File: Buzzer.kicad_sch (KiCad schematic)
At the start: 0 parts

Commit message: Pin out completion
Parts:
- added LS1: Speaker, symbol Device:Speaker
- added Q1: MMBT5551L, Package_TO_SOT_SMD:SOT-23, symbol Transistor_BJT:MMBT5551L
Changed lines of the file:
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@@
 		(comment 1 "天計")
 	)
+	(symbol
+		(lib_id "Transistor_BJT:MMBT5551L")
+		(at 119.38 101.6 0)
+		(unit 1)
+		(exclude_from_sim no)
+		(in_bom yes)
+		(on_board yes)
+		(dnp no)
+		(fields_autoplaced yes)
+		(property "Reference" "Q1"
+			(at 124.46 100.3299 0)
+			(effects
+				(font
+					(size 1.27 1.27)
+				)
+				(justify left)
+			)
+		)
+		(property "Value" "MMBT5551L"
+			(at 124.46 102.8699 0)
+			(effects
+				(font
+					(size 1.27 1.27)
+				)
+				(justify left)
+			)
+		)
+		(property "Footprint" "Package_TO_SOT_SMD:SOT-23"
+			(at 124.46 103.505 0)
+			(effects
+				(font
+					(size 1.27 1.27)
+					(italic yes)
+				)
+				(justify left)
+				(hide yes)
+			)
+		)
+		(property "Datasheet" "www.onsemi.com/pub/Collateral/MMBT5550LT1-D.PDF"
+			(at 119.38 101.6 0)
+			(effects
+				(font
+					(size 1.27 1.27)
+				)
+				(justify left)
+				(hide yes)
+			)
+		)
+		(property "Description" "0.6A Ic, 160V Vce, NPN Transistor, SOT-23"
+			(at 119.38 101.6 0)
+			(effects
+				(font
+					(size 1.27 1.27)
+				)
+				(hide yes)
+			)
+		)
+		(property "Sim.Device" "NPN"
+			(at 119.38 101.6 0)
+			(effects
+				(font
+					(size 1.27 1.27)
+				)
+				(hide yes)
+			)
+		)
+		(property "Sim.Pins" "1=B 2=E 3=C"
+			(at 119.38 101.6 0)
+			(effects
+				(font
+					(size 1.27 1.27)
+				)
+				(hide yes)
+			)
+		)
+		(pin "1"
+		)
+		(pin "3"
+		)
+		(pin "2"
+		)
+		(instances
+			(project ""
+				(path "/c9a8ff63-a0d1-4125-9dd1-40fb53daf536/fa1772ae-d612-479d-9fc0-6f13b32ea30c"
+					(reference "Q1")
+					(unit 1)
+				)
+			)
+		)
+	)
+	(symbol
+		(lib_id "Device:Speaker")
+		(at 129.54 74.93 0)
+		(unit 1)
+		(exclude_from_sim no)
+		(in_bom yes)
+		(on_board yes)
+		(dnp no)
+		(fields_autoplaced yes)
+		(property "Reference" "LS1"
+			(at 134.62 74.9299 0)
+			(effects
+				(font
+					(size 1.27 1.27)
+				)
+				(justify left)
+			)
+		)
+		(property "Value" "Speaker"
+			(at 134.62 77.4699 0)
+			(effects
+				(font
+					(size 1.27 1.27)
+				)
+				(justify left)
+			)
+		)
+		(property "Footprint" ""
+			(at 129.54 80.01 0)
+			(effects
+				(font
+					(size 1.27 1.27)
+				)
+				(hide yes)
+			)
+		)
+		(property "Datasheet" "~"
+			(at 129.286 76.2 0)
+			(effects
+				(font
+					(size 1.27 1.27)
+				)
+				(hide yes)
+			)
+		)
+		(property "Description" "Speaker"
+			(at 129.54 74.93 0)
+			(effects
+				(font
+					(size 1.27 1.27)
+				)
+				(hide yes)
+			)
+		)
+		(pin "1"
+		)
+		(pin "2"
+		)
+		(instances
+			(project ""
+				(path "/c9a8ff63-a0d1-4125-9dd1-40fb53daf536/fa1772ae-d612-479d-9fc0-6f13b32ea30c"
+					(reference "LS1")
+					(unit 1)
+				)
+			)
+		)
+	)
 )

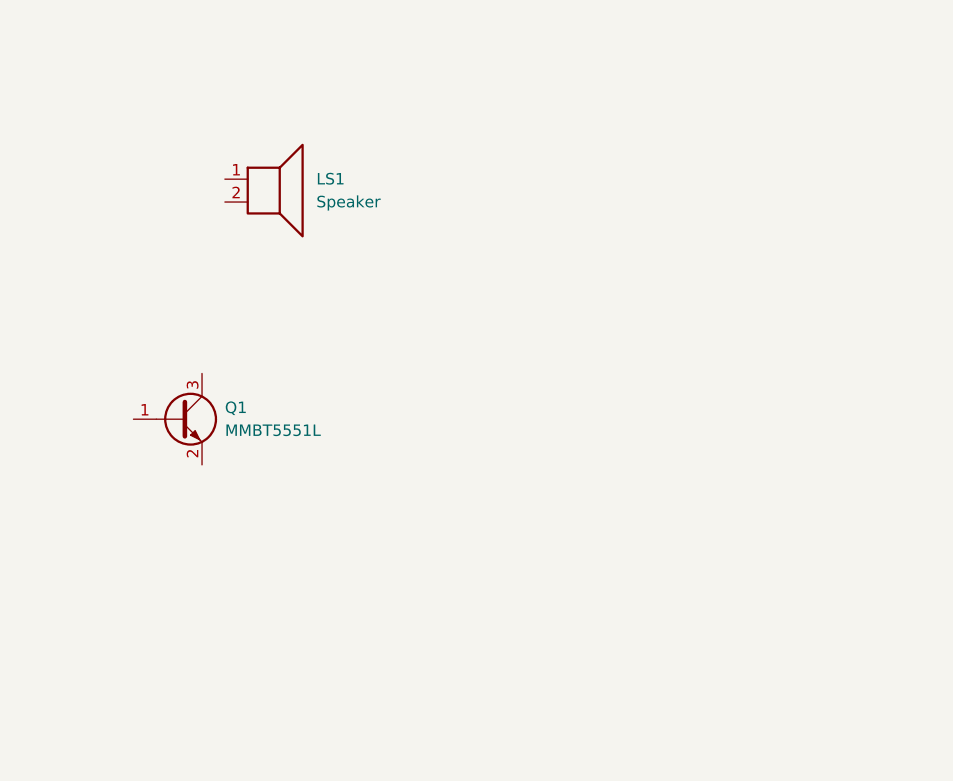
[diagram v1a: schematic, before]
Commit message: buzzer and ambient light sensor added
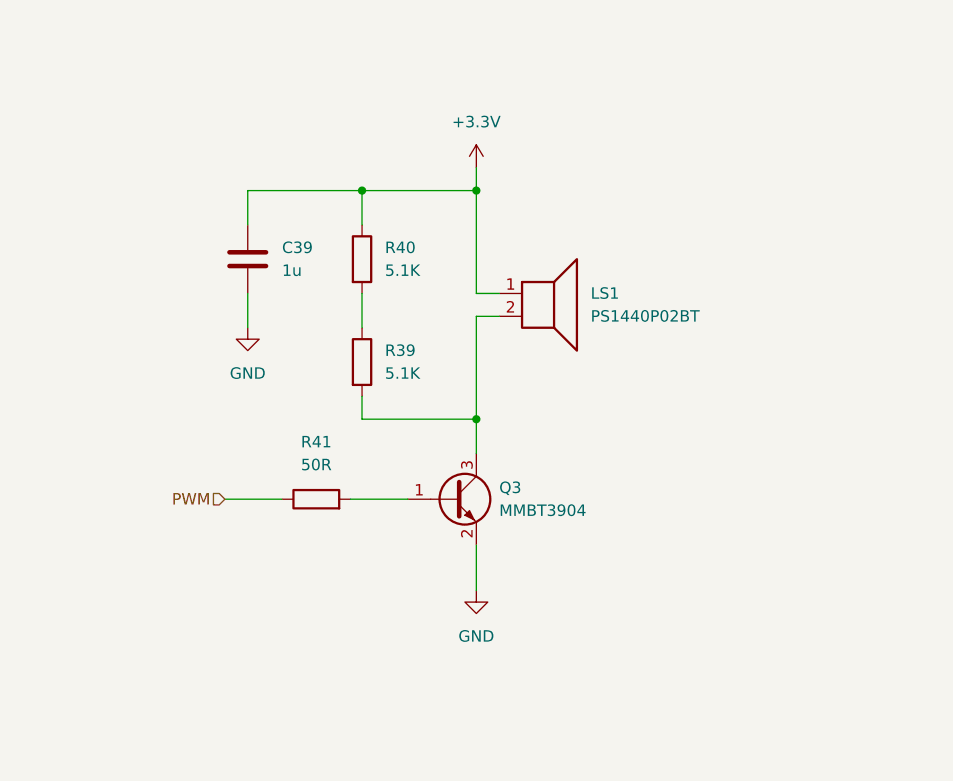
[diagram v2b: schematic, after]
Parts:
- removed Q1: MMBT5551L, Package_TO_SOT_SMD:SOT-23, symbol Transistor_BJT:MMBT5551L
- added C39: 1u, Capacitor_SMD:C_0603_1608Metric, symbol Device:C
- added Q3: MMBT3904, Package_TO_SOT_SMD:SOT-23, symbol Transistor_BJT:MMBT3904
- added R39, R40: 5.1K, Resistor_SMD:R_0402_1005Metric, symbol Device:R
- added R41: 50R, symbol Device:R
- LS1: value Speaker -> PS1440P02BT; footprint (none) -> precision_clock:TDK PS1440P02BT
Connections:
- net +3.3V: now reaches LS1.1
- net +3.3V: now also C39.1, R40.1
- net at LS1.2: now also Q3.3 (C), R39.2
- new net: Q3.1 (B), R41.2
- new net: R39.1, R40.2
- new net GND: C39.2, Q3.2 (E)
- new net PWM: R41.1
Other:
- moved on the sheet: LS1

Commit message: addition of BME690
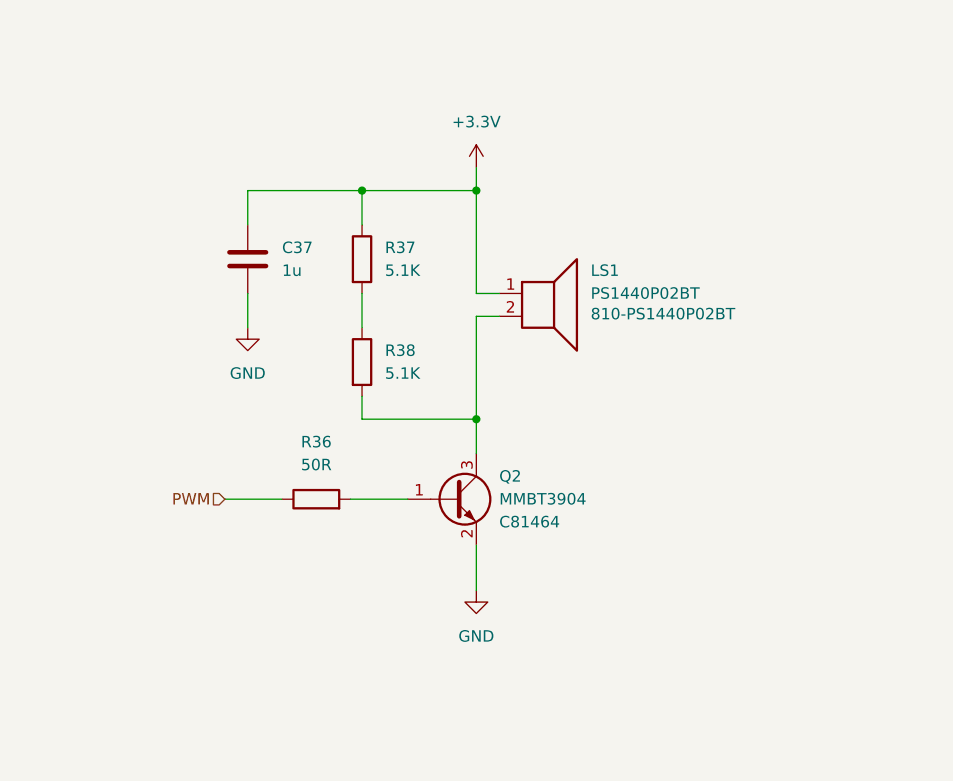
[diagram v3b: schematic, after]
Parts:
- LS1: Mouser (none) -> 810-PS1440P02BT
- Q2: renamed from Q3; LCSC (none) -> C81464
- R36: renamed from R41; footprint (none) -> Resistor_SMD:R_0402_1005Metric
- renumbered C39 to C37, R40 to R37, R39 to R38
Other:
- title: (none) -> Buzzer
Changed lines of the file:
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@@
 	(paper "A4")
 	(title_block
-		(date "2026-01-25")
+		(title "Buzzer")
+		(date "2026-01-27")
 		(rev "v0.0")
 		(company "TJ71PL")
 		(comment 1 "天計")
+		(comment 4 "Final verification incomplete")
 	)
 	(junction
@@
 		(on_board yes)
 		(dnp no)
-		(fields_autoplaced yes)
-		(property "Reference" "Q3"
-			(at 154.94 109.2199 0)
+		(property "Reference" "Q2"
+			(at 154.94 107.9501 0)
 			(effects
 				(font
@@
 		)
 		(property "Value" "MMBT3904"
-			(at 154.94 111.7599 0)
+			(at 154.94 110.49 0)
 			(effects
 				(font
@@
 			)
 		)
+		(property "LCSC" "C81464"
+			(at 154.94 113.0301 0)
+			(effects
+				(font
+					(size 1.27 1.27)
+				)
+				(justify left)
+			)
+		)
 		(pin "2"
 		)
@@
 			(project ""
 				(path "/c9a8ff63-a0d1-4125-9dd1-40fb53daf536/fa1772ae-d612-479d-9fc0-6f13b32ea30c"
-					(reference "Q3")
+					(reference "Q2")
 					(unit 1)
 				)
@@
 		(dnp no)
 		(fields_autoplaced yes)
-		(property "Reference" "R41"
+		(property "Reference" "R36"
 			(at 134.62 104.14 90)
 			(effects
@@
 			)
 		)
-		(property "Footprint" ""
+		(property "Footprint" "Resistor_SMD:R_0402_1005Metric"
 			(at 134.62 112.268 90)
 			(effects
@@
 			(project ""
 				(path "/c9a8ff63-a0d1-4125-9dd1-40fb53daf536/fa1772ae-d612-479d-9fc0-6f13b32ea30c"
-					(reference "R41")
+					(reference "R36")
 					(unit 1)
 				)
@@
 		(dnp no)
 		(fields_autoplaced yes)
-		(property "Reference" "C39"
+		(property "Reference" "C37"
 			(at 130.81 82.5499 0)
 			(effects
@@
 			(project "Precision Clock"
 				(path "/c9a8ff63-a0d1-4125-9dd1-40fb53daf536/fa1772ae-d612-479d-9fc0-6f13b32ea30c"
-					(reference "C39")
+					(reference "C37")
 					(unit 1)
 				)
@@
 		(dnp no)
 		(fields_autoplaced yes)
-		(property "Reference" "#PWR098"
+		(property "Reference" "#PWR097"
 			(at 127 97.79 0)
 			(effects
@@
 			(project "Precision Clock"
 				(path "/c9a8ff63-a0d1-4125-9dd1-40fb53daf536/fa1772ae-d612-479d-9fc0-6f13b32ea30c"
-					(reference "#PWR098")
+					(reference "#PWR097")
 					(unit 1)
 				)
@@
 		(on_board yes)
 		(dnp no)
-		(fields_autoplaced yes)
 		(property "Reference" "LS1"
-			(at 165.1 87.6299 0)
+			(at 165.1 85.09 0)
 			(effects
 				(font
@@
 		)
 		(property "Value" "PS1440P02BT"
-			(at 165.1 90.1699 0)
+			(at 165.1 87.63 0)
 			(effects
 				(font
@@
 			)
 		)
+		(property "Mouser" "810-PS1440P02BT"
+			(at 165.1 89.9161 0)
+			(effects
+				(font
+					(size 1.27 1.27)
+				)
+				(justify left)
+			)
+		)
 		(pin "1"
 		)
@@
 		(dnp no)
 		(fields_autoplaced yes)
-		(property "Reference" "#PWR011"
+		(property "Reference" "#PWR0101"
 			(at 152.4 127 0)
 			(effects
@@
 			(project ""
 				(path "/c9a8ff63-a0d1-4125-9dd1-40fb53daf536/fa1772ae-d612-479d-9fc0-6f13b32ea30c"
-					(reference "#PWR011")
+					(reference "#PWR0101")
 					(unit 1)
 				)
@@
 		(dnp no)
 		(fields_autoplaced yes)
-		(property "Reference" "#PWR020"
+		(property "Reference" "#PWR098"
 			(at 152.4 77.47 0)
 			(effects
@@
 			(project ""
 				(path "/c9a8ff63-a0d1-4125-9dd1-40fb53daf536/fa1772ae-d612-479d-9fc0-6f13b32ea30c"
-					(reference "#PWR020")
+					(reference "#PWR098")
 					(unit 1)
 				)
@@
 		(dnp no)
 		(fields_autoplaced yes)
-		(property "Reference" "R40"
+		(property "Reference" "R37"
 			(at 142.24 82.5499 0)
 			(effects
@@
 			(project "Precision Clock"
 				(path "/c9a8ff63-a0d1-4125-9dd1-40fb53daf536/fa1772ae-d612-479d-9fc0-6f13b32ea30c"
-					(reference "R40")
+					(reference "R37")
 					(unit 1)
 				)
@@
 		(dnp no)
 		(fields_autoplaced yes)
-		(property "Reference" "R39"
+		(property "Reference" "R38"
 			(at 142.24 93.9799 0)
 			(effects
@@
 			(project "Precision Clock"
 				(path "/c9a8ff63-a0d1-4125-9dd1-40fb53daf536/fa1772ae-d612-479d-9fc0-6f13b32ea30c"
-					(reference "R39")
-					(unit 1)
-				)
+					(reference "R38")
+					(unit 1)
+				)

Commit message: Verification
- changed the piezo electric speaker.
- verified some schematics
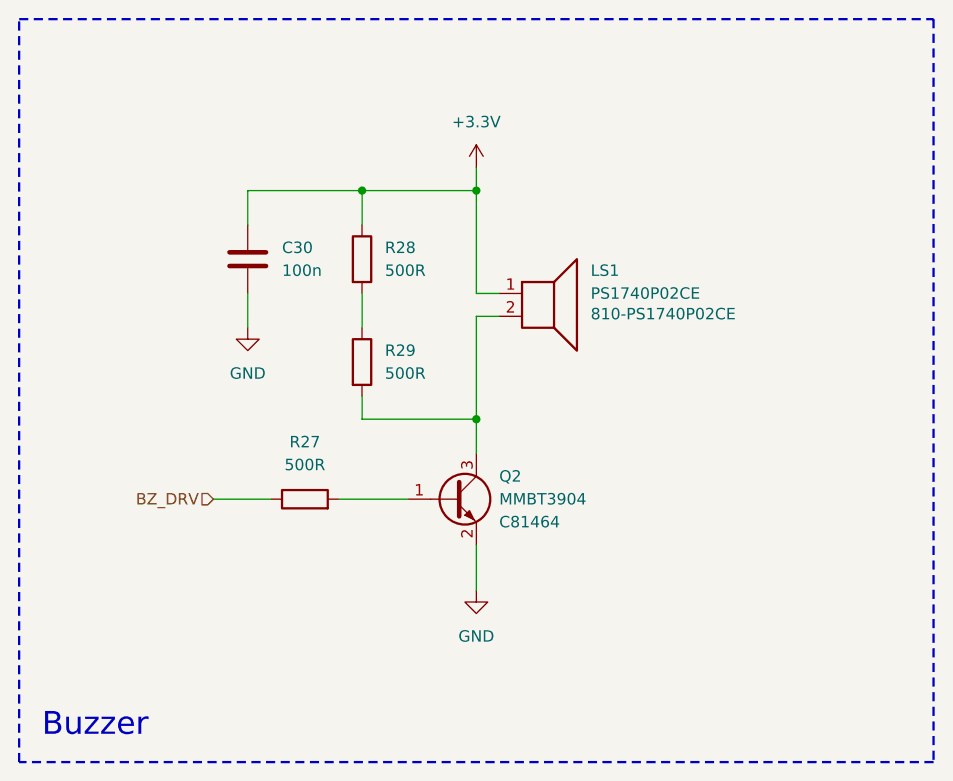
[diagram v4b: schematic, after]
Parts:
- removed C37: 1u, Capacitor_SMD:C_0603_1608Metric, symbol Device:C
- removed R37: 5.1K, Resistor_SMD:R_0402_1005Metric, symbol Device:R
- added C30: 100n, Capacitor_SMD:C_0402_1005Metric, symbol Device:C
- added R28: 500R, Resistor_SMD:R_0402_1005Metric, symbol Device:R
- LS1: value PS1440P02BT -> PS1740P02CE; footprint precision_clock:TDK PS1440P02BT -> precision_clock:TDK PS1740P02CE; Mouser 810-PS1440P02BT -> 810-PS1740P02CE
- R27: renamed from R36; value 50R -> 500R
- R29: renamed from R38; value 5.1K -> 500R
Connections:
- net +3.3V: now also C30.1, R28.1
- net GND: now also C30.2
- net at R29.1: now also R28.2
- net PWM renamed BZ_DRV
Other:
- note added: "Buzzer"
- moved on the sheet: R27

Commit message: Power subsystem updated
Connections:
- net BZ_DRV renamed BZ
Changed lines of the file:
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@@
 		)
 	)
-	(hierarchical_label "BZ_DRV"
+	(hierarchical_label "BZ"
 		(shape input)
 		(at 123.19 110.49 180)

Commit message: Verification
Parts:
- renumbered C30 to C33, R27 to R31, R28 to R32, R29 to R33
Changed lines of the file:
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@@
 	(title_block
 		(title "Buzzer")
-		(date "2026-01-29")
+		(date "2026-02-04")
 		(rev "v0.0")
 		(company "TJ71PL")
@@
 			(width 0.254)
 			(type dash)
-			(color 132 0 0 1)
 		)
 		(fill
@@
 				(size 2.54 2.54)
 				(thickness 0.3175)
-				(color 132 0 0 1)
 			)
 			(justify left)
@@
 			)
 		)
-		(column_widths 20.32)
+		(column_widths 17.78)
 		(row_heights 7.62 3.81 3.81 3.81 3.81 3.81 3.81)
 		(cells
@@
 				(exclude_from_sim no)
 				(at 180.34 106.68 0)
-				(size 20.32 7.62)
+				(size 17.78 7.62)
 				(margins 0.9525 0.9525 0.9525 0.9525)
 				(span 1 1)
@@
 				(exclude_from_sim no)
 				(at 180.34 114.3 0)
-				(size 20.32 3.81)
+				(size 17.78 3.81)
 				(margins 0.9525 0.9525 0.9525 0.9525)
 				(span 1 1)
@@
 				(exclude_from_sim no)
 				(at 180.34 118.11 0)
-				(size 20.32 3.81)
+				(size 17.78 3.81)
 				(margins 0.9525 0.9525 0.9525 0.9525)
 				(span 1 1)
@@
 				(exclude_from_sim no)
 				(at 180.34 121.92 0)
-				(size 20.32 3.81)
+				(size 17.78 3.81)
 				(margins 0.9525 0.9525 0.9525 0.9525)
 				(span 1 1)
@@
 				(exclude_from_sim no)
 				(at 180.34 125.73 0)
-				(size 20.32 3.81)
+				(size 17.78 3.81)
 				(margins 0.9525 0.9525 0.9525 0.9525)
 				(span 1 1)
@@
 				(exclude_from_sim no)
 				(at 180.34 129.54 0)
-				(size 20.32 3.81)
+				(size 17.78 3.81)
 				(margins 0.9525 0.9525 0.9525 0.9525)
 				(span 1 1)
@@
 				(exclude_from_sim no)
 				(at 180.34 133.35 0)
-				(size 20.32 3.81)
+				(size 17.78 3.81)
 				(margins 0.9525 0.9525 0.9525 0.9525)
 				(span 1 1)
@@
 		(on_board yes)
 		(dnp no)
-		(property "Reference" "C30"
+		(property "Reference" "C33"
 			(at 130.81 82.5499 0)
 			(effects
@@
 			(project "Precision Clock"
 				(path "/c9a8ff63-a0d1-4125-9dd1-40fb53daf536/fa1772ae-d612-479d-9fc0-6f13b32ea30c"
-					(reference "C30")
+					(reference "C33")
 					(unit 1)
 				)
@@
 		(dnp no)
 		(fields_autoplaced yes)
-		(property "Reference" "R27"
+		(property "Reference" "R31"
 			(at 133.35 104.14 90)
 			(effects
@@
 			(project ""
 				(path "/c9a8ff63-a0d1-4125-9dd1-40fb53daf536/fa1772ae-d612-479d-9fc0-6f13b32ea30c"
-					(reference "R27")
+					(reference "R31")
 					(unit 1)
 				)
@@
 		(dnp no)
 		(fields_autoplaced yes)
-		(property "Reference" "R28"
+		(property "Reference" "R32"
 			(at 142.24 82.5499 0)
 			(effects
@@
 			(project "Precision Clock"
 				(path "/c9a8ff63-a0d1-4125-9dd1-40fb53daf536/fa1772ae-d612-479d-9fc0-6f13b32ea30c"
-					(reference "R28")
+					(reference "R32")
 					(unit 1)
 				)
@@
 		(dnp no)
 		(fields_autoplaced yes)
-		(property "Reference" "#PWR080"
+		(property "Reference" "#PWR087"
 			(at 127 97.79 0)
 			(effects
@@
 			(project "Precision Clock"
 				(path "/c9a8ff63-a0d1-4125-9dd1-40fb53daf536/fa1772ae-d612-479d-9fc0-6f13b32ea30c"
-					(reference "#PWR080")
+					(reference "#PWR087")
 					(unit 1)
 				)
@@
 		(dnp no)
 		(fields_autoplaced yes)
-		(property "Reference" "#PWR079"
+		(property "Reference" "#PWR092"
 			(at 152.4 127 0)
 			(effects
@@
 			(project ""
 				(path "/c9a8ff63-a0d1-4125-9dd1-40fb53daf536/fa1772ae-d612-479d-9fc0-6f13b32ea30c"
-					(reference "#PWR079")
+					(reference "#PWR092")
 					(unit 1)
 				)
@@
 		(dnp no)
 		(fields_autoplaced yes)
-		(property "Reference" "#PWR076"
+		(property "Reference" "#PWR091"
 			(at 152.4 77.47 0)
 			(effects
@@
 			(project ""
 				(path "/c9a8ff63-a0d1-4125-9dd1-40fb53daf536/fa1772ae-d612-479d-9fc0-6f13b32ea30c"
-					(reference "#PWR076")
+					(reference "#PWR091")
 					(unit 1)
 				)
@@
 		(dnp no)
 		(fields_autoplaced yes)
-		(property "Reference" "R29"
+		(property "Reference" "R33"
 			(at 142.24 93.9799 0)
 			(effects
@@
 			(project "Precision Clock"
 				(path "/c9a8ff63-a0d1-4125-9dd1-40fb53daf536/fa1772ae-d612-479d-9fc0-6f13b32ea30c"
-					(reference "R29")
+					(reference "R33")
 					(unit 1)
 				)
